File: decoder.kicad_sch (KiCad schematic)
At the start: 30 parts

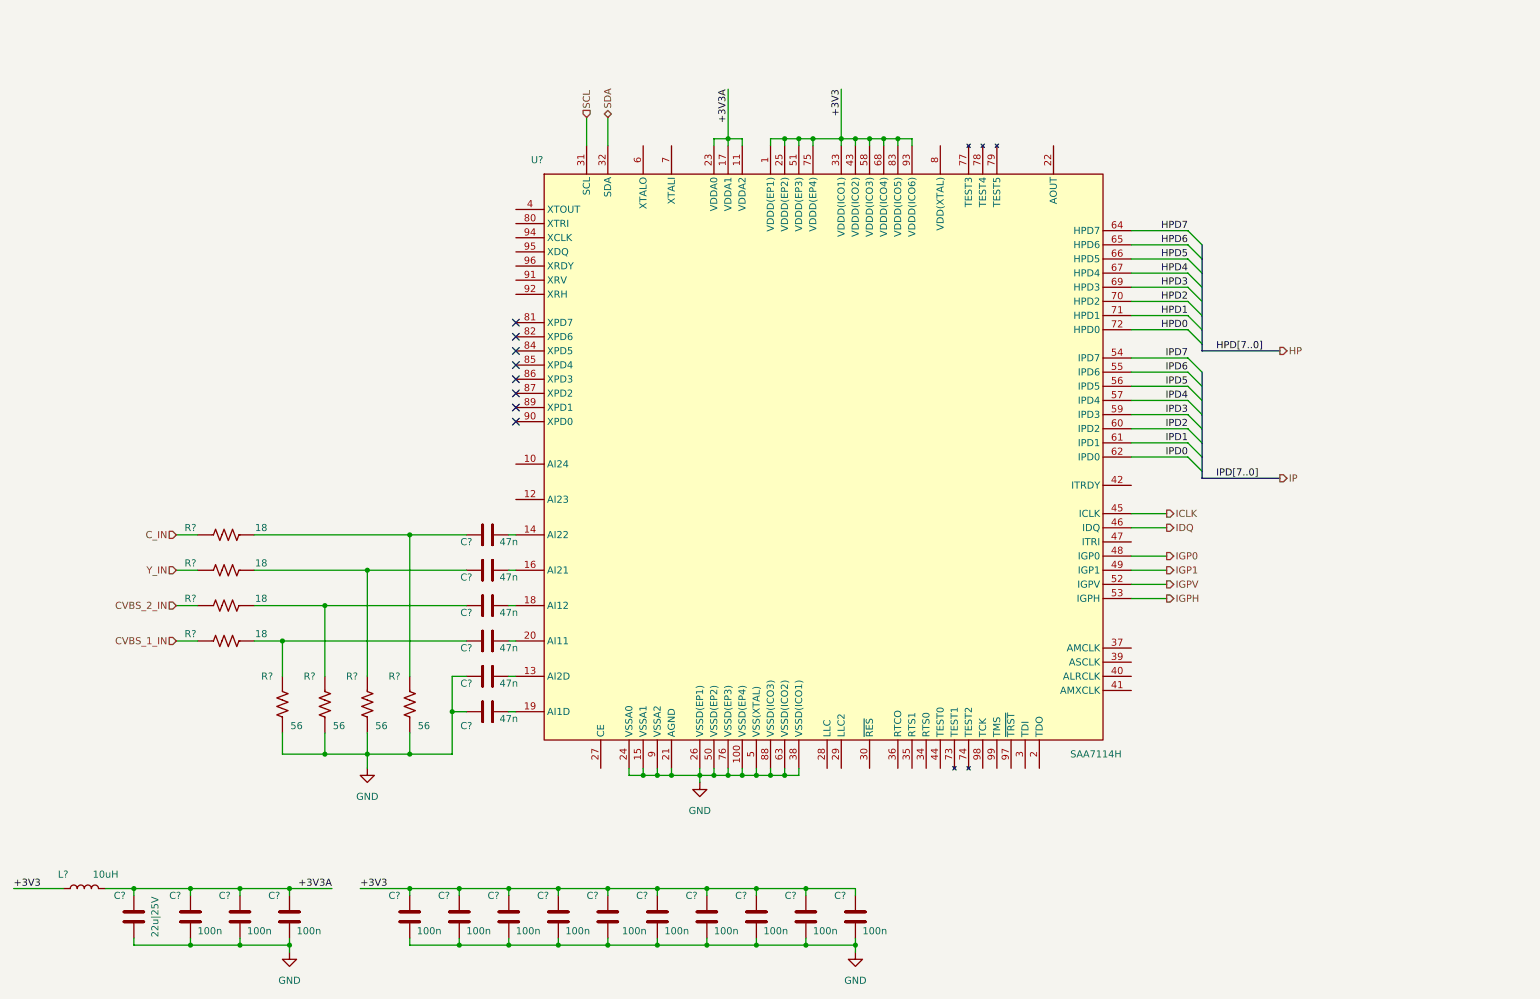
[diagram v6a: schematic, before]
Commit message: added connectors and crystal, osc
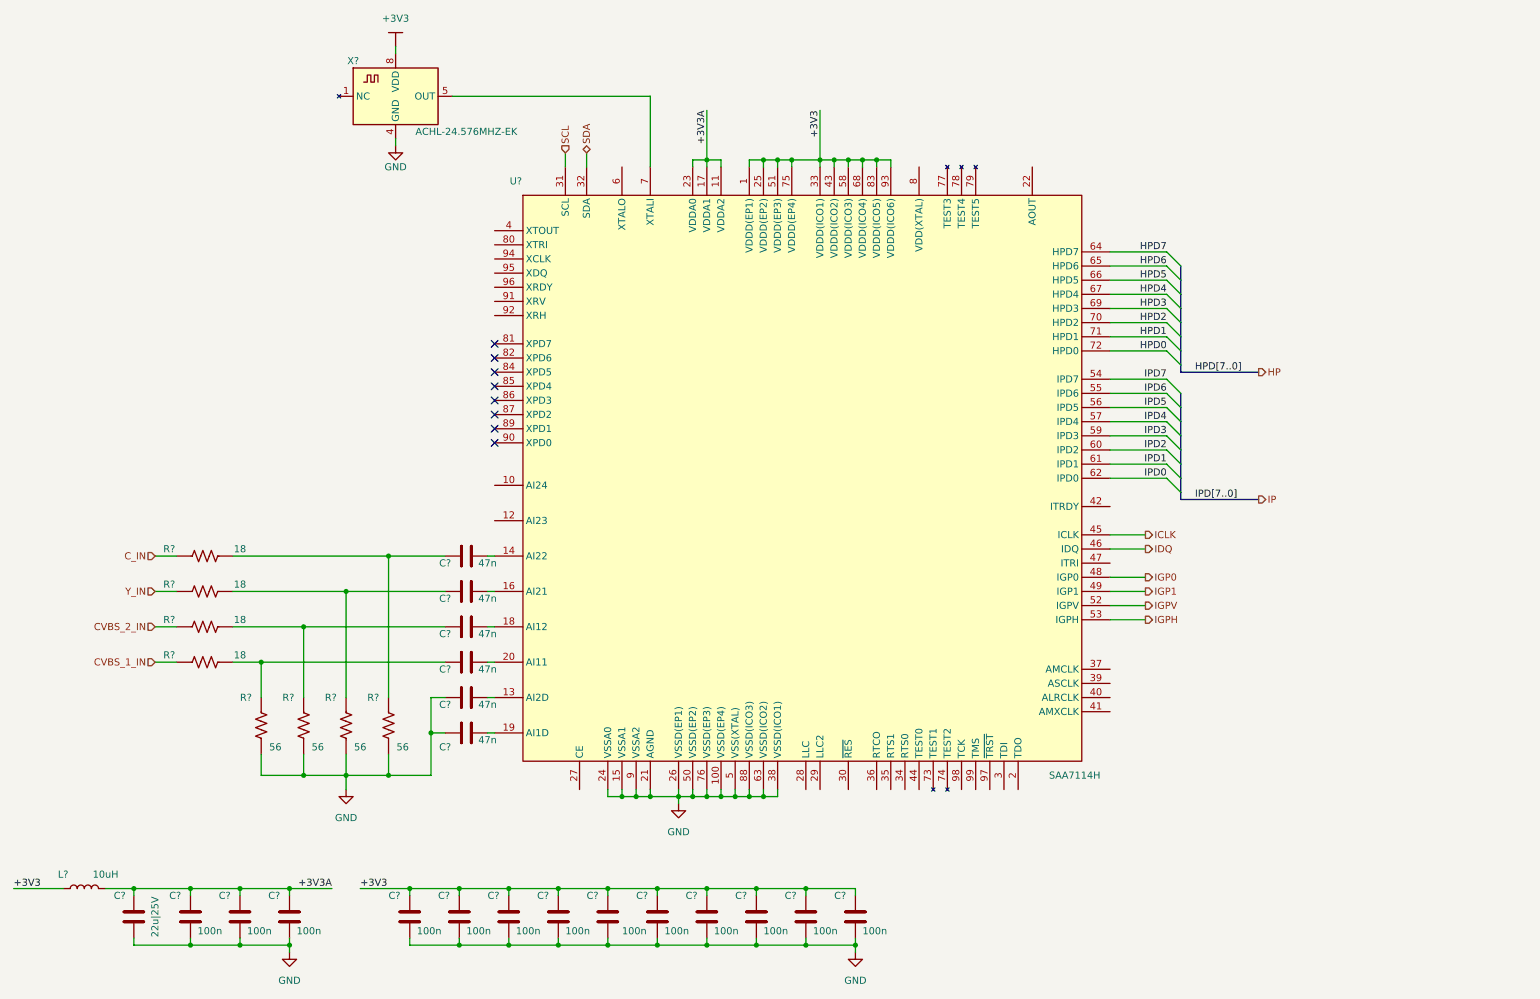
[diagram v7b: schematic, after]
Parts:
- added X?: ACHL-24.576MHZ-EK, symbol tbc:ACHL-24.576MHZ-EK
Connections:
- net +3V3: now also X?.8 (VDD)
- net GND: now also X?.4 (GND)
- net at U?.7 (XTALI): now also X?.5 (OUT)
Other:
- moved on the sheet: C?, R?, U?

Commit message: completed and annotated schematic, passed ERC
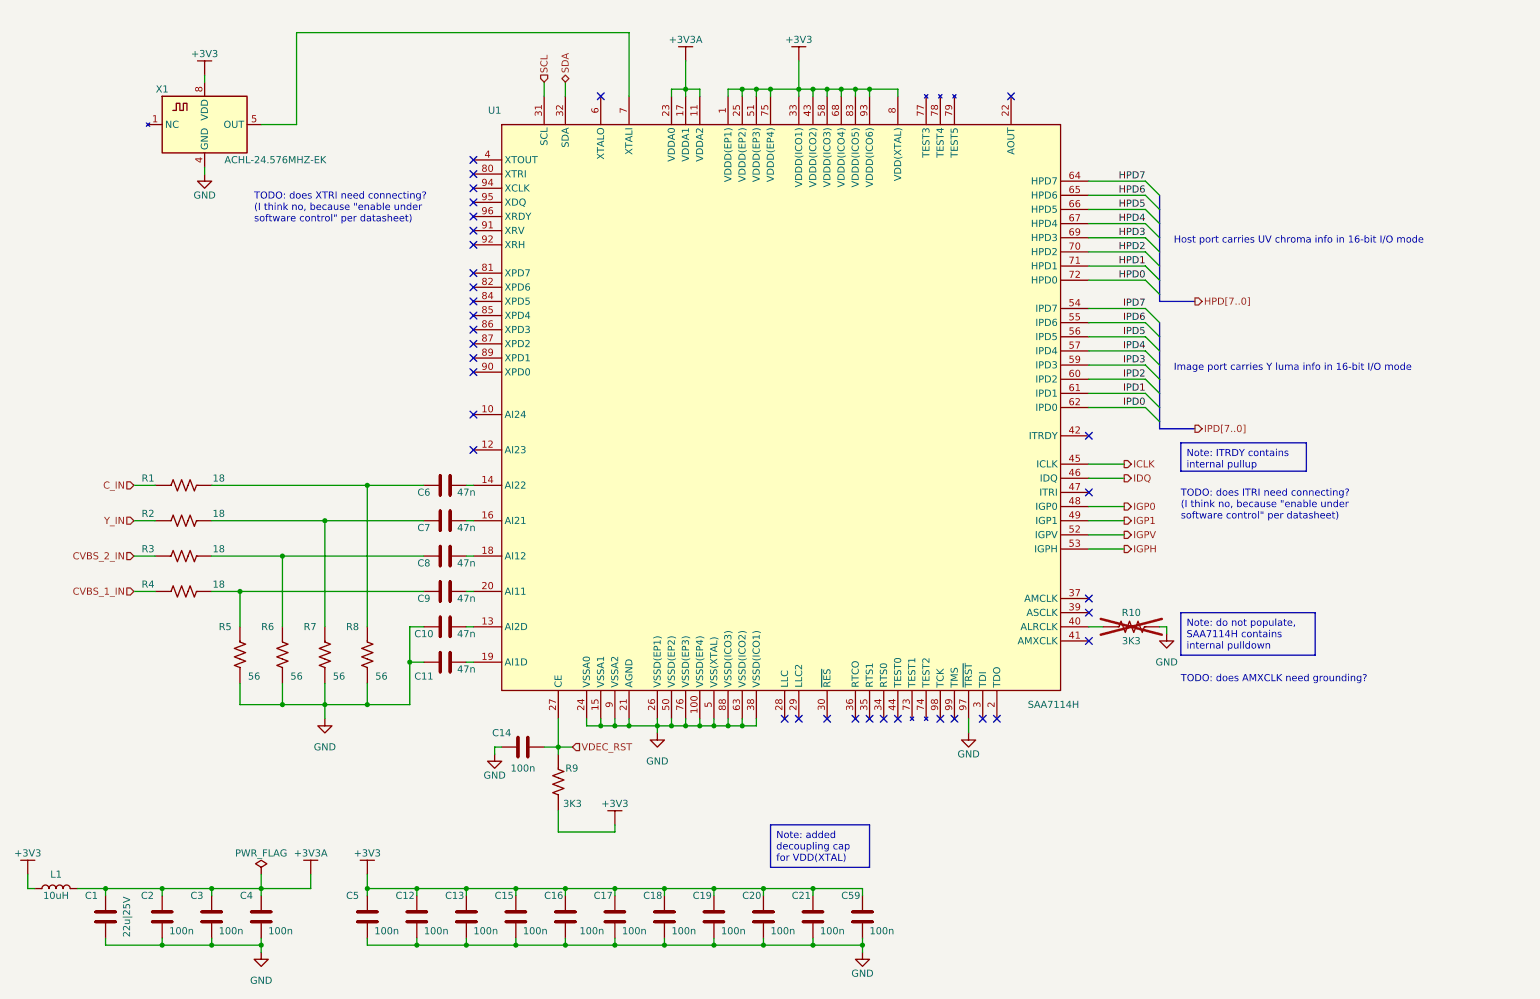
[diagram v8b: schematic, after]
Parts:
- added C14, C59: 100n, symbol tbc:GCJ188R71H104KA12D
- added R10, R9: 3K3, symbol tbc:RC0603FR-073K3L
- gave numbers to parts that had none: 31
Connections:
- net +3V3: now also U1.8 (VDD(XTAL)), C59.2, R9.1
- net GND: now also U1.97 (~{TRST}), C14.1, C59.1, R10.2
- net VDEC_RST: now reaches U1.27 (CE)
- net VDEC_RST: now also C14.2, R9.2
- net at U1.40 (ALRCLK): now also R10.1
- no-connect marks 8 -> 35
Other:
- note added: "Host port carries UV chroma info in 16-bit I/O mode"
- note added: "Image port carries Y luma info in 16-bit I/O mode"
- note added: "TODO: does AMXCLK need grounding?"
- note added: "TODO: does ITRI need connecting? (I think no, because "enable under software control" per datasheet)"
- note added: "TODO: does XTRI need connecting? (I think no, because "enable under software control" per datasheet)"
- moved on the sheet: C1, C10, C11, C12, C13, C15, C16, C17, C18, C19, C2, C20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
